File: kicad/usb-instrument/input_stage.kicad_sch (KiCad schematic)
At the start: 24 parts, among them U2 ADS131M02IRUKR, U3 LM317_SOT-223, U9 TLV172IDCK, Y1 XO32

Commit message: begin layout
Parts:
- C1, C13, C2: footprint (none) -> Capacitor_SMD:C_0805_2012Metric_Pad1.18x1.45mm_HandSolder
- R1, R2, R3, R4, R7, R9: footprint (none) -> Resistor_SMD:R_0805_2012Metric_Pad1.20x1.40mm_HandSolder
- U2: footprint WQFN20_ADS131_TEX -> Footprints:WQFN20_ADS131_TEX
- Y1: footprint (none) -> Crystal:Crystal_SMD_7050-4Pin_7.0x5.0mm
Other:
- moved on the sheet: C16, C3, D4, R13, R7, U9

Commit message: geroutet
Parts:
- added R10: 10k, Resistor_SMD:R_0805_2012Metric_Pad1.20x1.40mm_HandSolder, symbol Device:R
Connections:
- net GNDA: no longer R9.1
- net R_SENSE: now also R1.1; no longer R3.1
- net SYNC/RESET: now also R10.1
- net VIN_3.3V: now also R9.1, R10.2
- net V_PD: now also R3.1; no longer R1.1
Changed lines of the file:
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@@
 	(wire
 		(pts
-			(xy 109.22 68.58) (xy 110.49 68.58)
+			(xy 260.35 62.23) (xy 223.52 62.23)
 		)
 		(stroke
@@
 	(wire
 		(pts
-			(xy 260.35 62.23) (xy 223.52 62.23)
+			(xy 248.92 67.31) (xy 223.52 67.31)
 		)
 		(stroke
@@
 	(wire
 		(pts
-			(xy 248.92 67.31) (xy 223.52 67.31)
+			(xy 106.68 118.11) (xy 96.52 118.11)
 		)
 		(stroke
@@
 	(wire
 		(pts
-			(xy 106.68 118.11) (xy 96.52 118.11)
+			(xy 96.52 138.43) (xy 96.52 137.16)
 		)
 		(stroke
@@
 	(wire
 		(pts
-			(xy 96.52 138.43) (xy 96.52 137.16)
+			(xy 124.46 45.72) (xy 118.11 45.72)
 		)
 		(stroke
@@
 	(wire
 		(pts
-			(xy 124.46 45.72) (xy 118.11 45.72)
+			(xy 63.5 67.31) (xy 53.34 67.31)
 		)
 		(stroke
@@
 	(wire
 		(pts
-			(xy 63.5 67.31) (xy 53.34 67.31)
+			(xy 101.6 68.58) (xy 110.49 68.58)
 		)
 		(stroke
@@
 	(wire
 		(pts
+			(xy 109.22 45.72) (xy 110.49 45.72)
+		)
+		(stroke
+			(width 0)
+			(type default)
+		)
+	)
+	(wire
+		(pts
 			(xy 104.14 132.08) (xy 105.41 132.08)
 		)
@@
 		)
 	)
-	(wire
-		(pts
-			(xy 101.6 45.72) (xy 110.49 45.72)
-		)
-		(stroke
-			(width 0)
-			(type default)
-		)
-	)
 	(label "CLKIN"
 		(at 229.87 69.85 180)
@@
 		)
 	)
-	(label "V_PD"
-		(at 101.6 45.72 0)
-		(effects
-			(font
-				(size 1.27 1.27)
-			)
-			(justify left bottom)
-		)
-	)
 	(label "AIN1P"
 		(at 124.46 68.58 180)
@@
 		)
 	)
+	(label "DVDD"
+		(at 161.29 67.31 180)
+		(effects
+			(font
+				(size 1.27 1.27)
+			)
+			(justify right bottom)
+		)
+	)
+	(label "DVDD"
+		(at 156.21 77.47 180)
+		(effects
+			(font
+				(size 1.27 1.27)
+			)
+			(justify right bottom)
+		)
+	)
 	(label "V_PD"
 		(at 129.54 134.62 180)
@@
 		)
 	)
+	(label "V_PD"
+		(at 101.6 68.58 0)
+		(effects
+			(font
+				(size 1.27 1.27)
+			)
+			(justify left bottom)
+		)
+	)
 	(label "DVDD"
 		(at 46.99 26.67 180)
@@
 		)
 	)
-	(hierarchical_label "SYNC{slash}RESET"
+	(hierarchical_label "R_SENSE"
 		(shape input)
-		(at 161.29 74.93 180)
+		(at 109.22 45.72 180)
 		(effects
 			(font
@@
 		)
 	)
-	(hierarchical_label "R_SENSE"
+	(hierarchical_label "GNDA"
 		(shape input)
-		(at 109.22 68.58 180)
+		(at 52.07 67.31 180)
 		(effects
 			(font
@@
 		)
 	)
-	(hierarchical_label "GNDA"
+	(hierarchical_label "SYNC{slash}RESET"
 		(shape input)
-		(at 52.07 67.31 180)
+		(at 161.29 74.93 180)
 		(effects
 			(font
@@
 	)
 	(symbol
+		(lib_id "Device:R")
+		(at 161.29 71.12 180)
+		(unit 1)
+		(body_style 1)
+		(exclude_from_sim no)
+		(in_bom yes)
+		(on_board yes)
+		(in_pos_files yes)
+		(dnp no)
+		(property "Reference" "R10"
+			(at 161.29 71.12 90)
+			(show_name no)
+			(do_not_autoplace no)
+			(effects
+				(font
+					(size 1.27 1.27)
+				)
+			)
+		)
+		(property "Value" "10k"
+			(at 163.83 71.12 90)
+			(show_name no)
+			(do_not_autoplace no)
+			(effects
+				(font
+					(size 1.27 1.27)
+				)
+			)
+		)
+		(property "Footprint" "Resistor_SMD:R_0805_2012Metric_Pad1.20x1.40mm_HandSolder"
+			(at 163.068 71.12 90)
+			(hide yes)
+			(show_name no)
+			(do_not_autoplace no)
+			(effects
+				(font
+					(size 1.27 1.27)
+				)
+			)
+		)
+		(property "Datasheet" ""
+			(at 161.29 71.12 0)
+			(hide yes)
+			(show_name no)
+			(do_not_autoplace no)
+			(effects
+				(font
+					(size 1.27 1.27)
+				)
+			)
+		)
+		(property "Description" "Resistor"
+			(at 161.29 71.12 0)
+			(hide yes)
+			(show_name no)
+			(do_not_autoplace no)
+			(effects
+				(font
+					(size 1.27 1.27)
+				)
+			)
+		)
+		(pin "1"
+		)
+		(pin "2"
+		)
+		(instances
+			(project "usb-instrument"
+				(path "/e3f69e86-1123-464e-9947-982c7ad4894b/3bb653df-7c32-4163-b60c-aea8374e41b3"
+					(reference "R10")
+					(unit 1)
+				)
+			)
+		)
+	)
+	(symbol
 		(lib_id "power:GNDA")
 		(at 223.52 64.77 90)
@@
 					(unit 1)
 				)
-			)
-		)
-	)
-	(symbol
-		(lib_id "power:GNDA")
-		(at 156.21 77.47 270)
-		(unit 1)
-		(body_style 1)
-		(exclude_from_sim no)
-		(in_bom yes)
-		(on_board yes)
-		(in_pos_files yes)
-		(dnp no)
-		(property "Reference" "#PWR062"
-			(at 149.86 77.47 0)
-			(hide yes)
-			(show_name no)
-			(do_not_autoplace no)
-			(effects
-				(font
-					(size 1.27 1.27)
-				)
-			)
-		)
-		(property "Value" "GNDA"
-			(at 150.876 77.47 90)
-			(show_name no)
-			(do_not_autoplace no)
-			(effects
-				(font
-					(size 1.27 1.27)
-				)
-			)
-		)
-		(property "Footprint" ""
-			(at 156.21 77.47 0)
-			(hide yes)
-			(show_name no)
-			(do_not_autoplace no)
-			(effects
-				(font
-					(size 1.27 1.27)
-				)
-			)
-		)
-		(property "Datasheet" ""
-			(at 156.21 77.47 0)
-			(hide yes)
-			(show_name no)
-			(do_not_autoplace no)
-			(effects
-				(font
-					(size 1.27 1.27)
-				)
-			)
-		)
-		(property "Description" "Power symbol creates a global label with name \"GNDA\" , analog ground"
-			(at 156.21 77.47 0)
-			(hide yes)
-			(show_name no)
-			(do_not_autoplace no)
-			(effects
-				(font
-					(size 1.27 1.27)
-				)
-			)
-		)
-		(pin "1"
-		)
-		(instances
-			(project "usb-instrument"
-				(path "/e3f69e86-1123-464e-9947-982c7ad4894b/3bb653df-7c32-4163-b60c-aea8374e41b3"
-					(reference "#PWR062")
-					(unit 1)
-				)

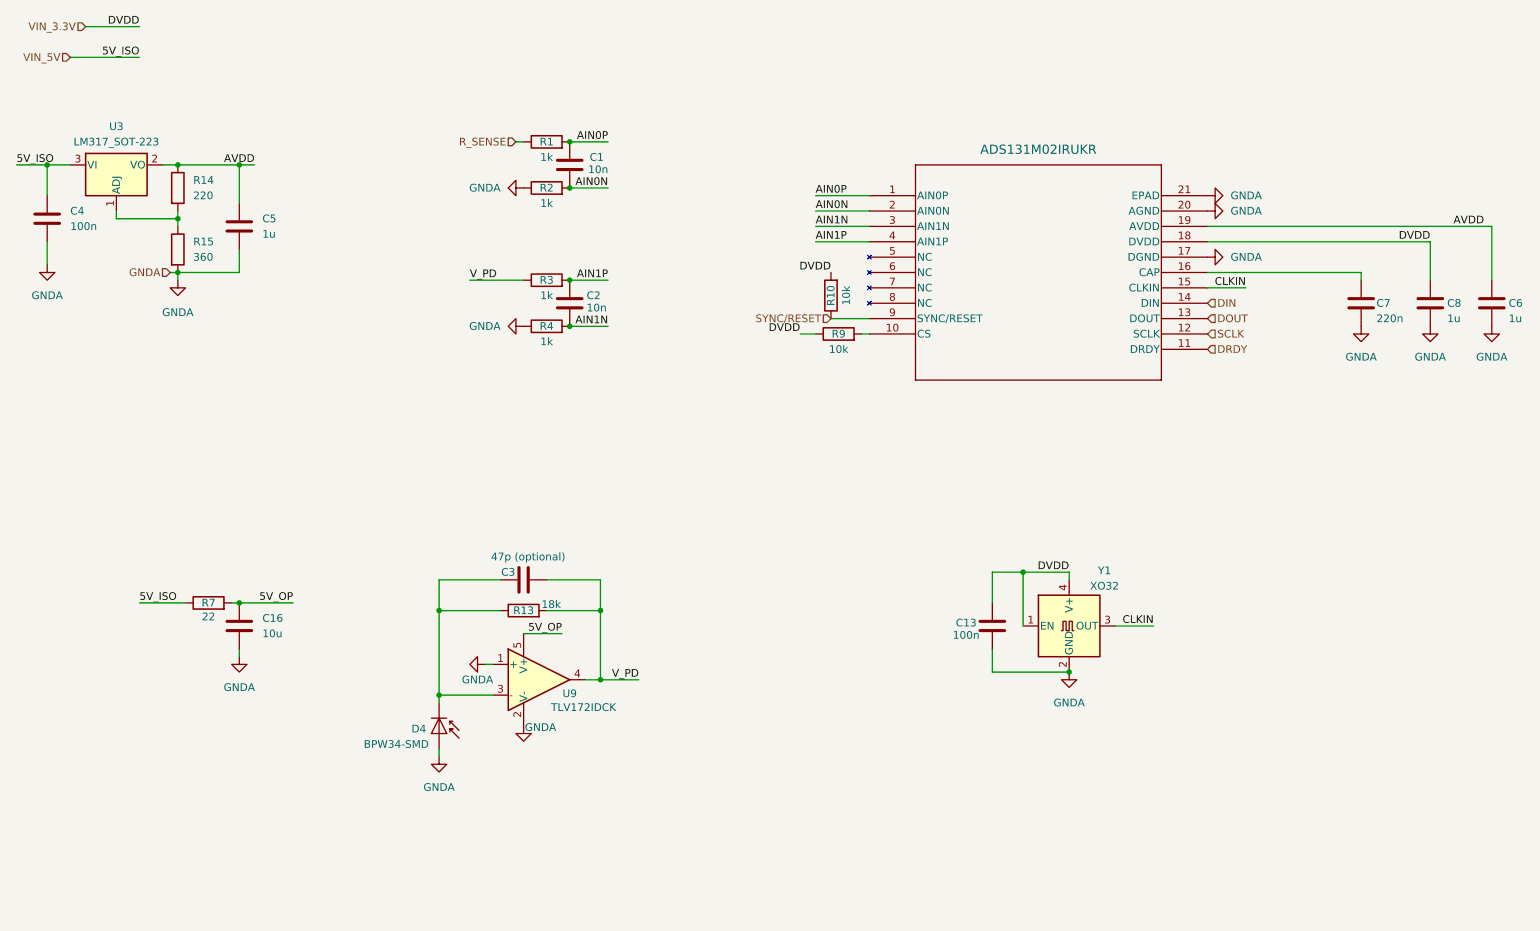
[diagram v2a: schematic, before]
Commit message: updated footprints
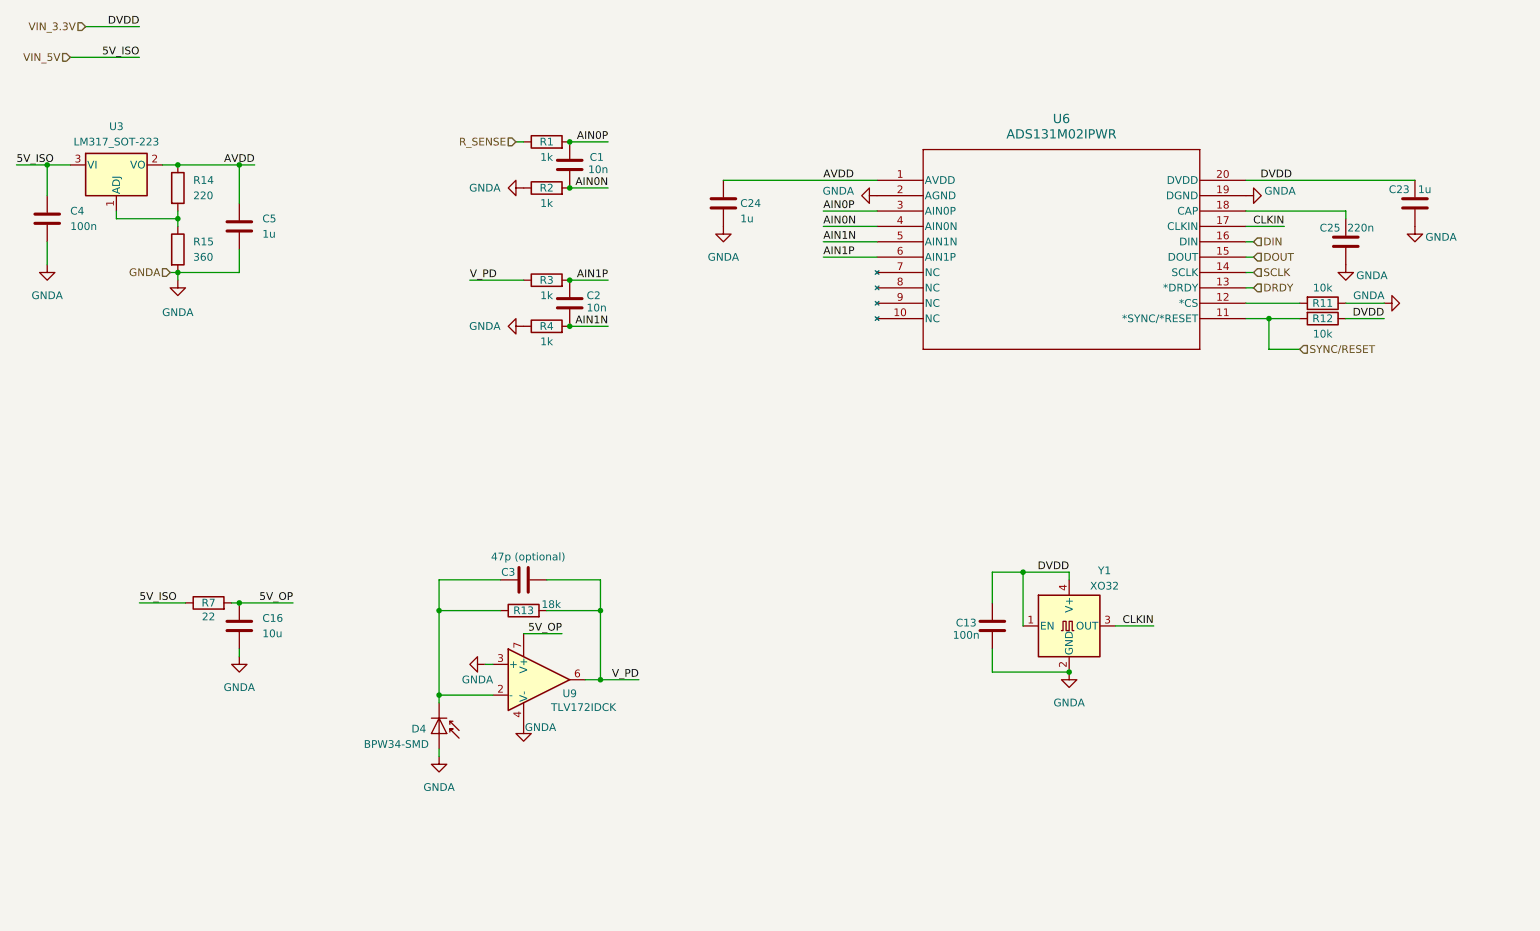
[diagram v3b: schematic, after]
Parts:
- removed C6, C8: 1u, Capacitor_SMD:C_0805_2012Metric_Pad1.18x1.45mm_HandSolder, symbol Device:C
- removed C7: 220n, Capacitor_SMD:C_0805_2012Metric_Pad1.18x1.45mm_HandSolder, symbol Device:C
- removed R10, R9: 10k, Resistor_SMD:R_0805_2012Metric_Pad1.20x1.40mm_HandSolder, symbol Device:R
- removed U2: ADS131M02IRUKR, Footprints:WQFN20_ADS131_TEX, symbol Symbols:ADS131M02IRUKR
- added C23, C24: 1u, Capacitor_SMD:C_0805_2012Metric_Pad1.18x1.45mm_HandSolder, symbol Device:C
- added C25: 220n, Capacitor_SMD:C_0805_2012Metric_Pad1.18x1.45mm_HandSolder, symbol Device:C
- added R11, R12: 10k, Resistor_SMD:R_0805_2012Metric_Pad1.20x1.40mm_HandSolder, symbol Device:R
- added U6: ADS131M02IPWR, Footprints:TSSOP20_PW_TEX, symbol Symbols:ADS131M02IPWR
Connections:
- net 5V_OP: now also U9.7 (V+); no longer U9.5 (V+)
- net AIN0N: now also U6.4 (AIN0N)
- net AIN0P: now also U6.3 (AIN0P)
- net AIN1N: now also U6.5 (AIN1N)
- net AIN1P: now also U6.6 (AIN1P)
- net AVDD: now also C24.1, U6.1 (AVDD)
- net CLKIN: now also U6.17 (CLKIN)
- net DIN: now also U6.16 (DIN)
- net DOUT: now also U6.15 (DOUT)
- net DRDY: now also U6.13 (*DRDY)
- net GNDA: now also U9.3 (+), U9.4 (V-), C23.2, C24.2, C25.2, R11.1, U6.19 (DGND), U6.2 (AGND); no longer U9.1 (+), U9.2 (V-)
- net SCLK: now also U6.14 (SCLK)
- net SYNC/RESET: now also R12.2, U6.11 (*SYNC/*RESET)
- net VIN_3.3V: now also C23.1, R12.1, U6.20 (DVDD)
- net V_PD: now also U9.6; no longer U9.4
- net at C3.1, D4.1 (K), R13.1: now also U9.2 (-); no longer U9.3 (-)
- new net: R11.2, U6.12 (*CS)
- new net: C25.1, U6.18 (CAP)
